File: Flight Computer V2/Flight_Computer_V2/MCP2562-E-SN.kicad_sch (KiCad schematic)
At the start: 2 parts, among them U3 MCP2562-E-SN

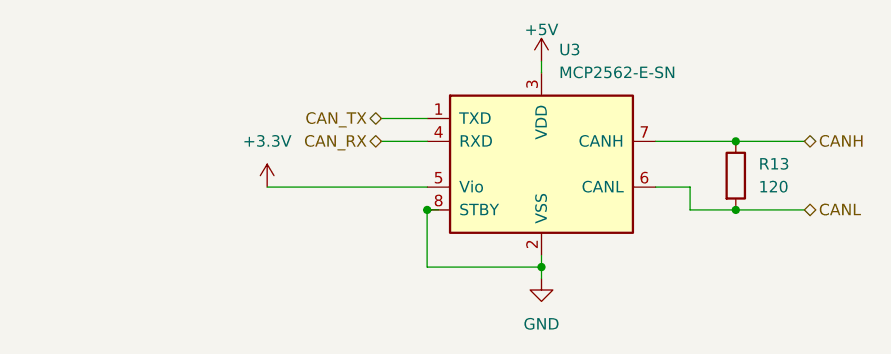
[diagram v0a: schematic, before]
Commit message: added more sensors to flight computer v2
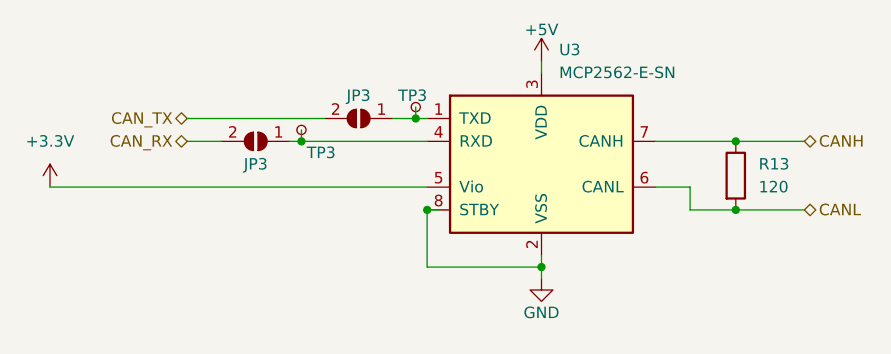
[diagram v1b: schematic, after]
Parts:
- added JP3 (x2): ~, symbol Jumper:SolderJumper_2_Open
- added TP3 (x2): TestPoint_Small, symbol Connector:TestPoint_Small
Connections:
- net CAN_RX: now also JP3.2 (B); no longer U3.4 (RXD)
- net CAN_TX: now also JP3.2 (B); no longer U3.1 (TXD)
- new net: JP3.1 (A), TP3.1, U3.1 (TXD)
- new net: JP3.1 (A), TP3.1, U3.4 (RXD)
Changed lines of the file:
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@@
   (junction (at 153.67 99.06) (diameter 0) (color 0 0 0 0)
   )
+  (junction (at 118.11 88.9) (diameter 0) (color 0 0 0 0)
+  )
+  (junction (at 105.41 91.44) (diameter 0) (color 0 0 0 0)
+  )
   (junction (at 119.38 99.06) (diameter 0) (color 0 0 0 0)
   )
+  (wire (pts (xy 115.57 88.9) (xy 118.11 88.9))
+    (stroke (width 0) (type default))
+  )
   (wire (pts (xy 132.08 82.55) (xy 132.08 83.82))
     (stroke (width 0) (type default))
@@
     (stroke (width 0) (type default))
   )
+  (wire (pts (xy 104.14 91.44) (xy 105.41 91.44))
+    (stroke (width 0) (type default))
+  )
   (wire (pts (xy 119.38 105.41) (xy 132.08 105.41))
     (stroke (width 0) (type default))
   )
+  (wire (pts (xy 105.41 91.44) (xy 119.38 91.44))
+    (stroke (width 0) (type default))
+  )
   (wire (pts (xy 144.78 96.52) (xy 148.59 96.52))
     (stroke (width 0) (type default))
@@
     (stroke (width 0) (type default))
   )
-  (wire (pts (xy 101.6 96.52) (xy 119.38 96.52))
-    (stroke (width 0) (type default))
-  )
-  (wire (pts (xy 114.3 88.9) (xy 119.38 88.9))
+  (wire (pts (xy 92.71 88.9) (xy 107.95 88.9))
+    (stroke (width 0) (type default))
+  )
+  (wire (pts (xy 105.41 90.17) (xy 105.41 91.44))
+    (stroke (width 0) (type default))
+  )
+  (wire (pts (xy 118.11 87.63) (xy 118.11 88.9))
+    (stroke (width 0) (type default))
+  )
+  (wire (pts (xy 118.11 88.9) (xy 119.38 88.9))
     (stroke (width 0) (type default))
   )
@@
     (stroke (width 0) (type default))
   )
+  (wire (pts (xy 77.47 96.52) (xy 119.38 96.52))
+    (stroke (width 0) (type default))
+  )
   (wire (pts (xy 148.59 99.06) (xy 153.67 99.06))
     (stroke (width 0) (type default))
   )
-  (wire (pts (xy 114.3 91.44) (xy 119.38 91.44))
+  (wire (pts (xy 92.71 91.44) (xy 96.52 91.44))
     (stroke (width 0) (type default))
   )
@@
     (effects (font (size 1.27 1.27)) (justify left))
   )
-  (hierarchical_label "CAN_TX" (shape bidirectional) (at 114.3 88.9 180) (fields_autoplaced)
+  (hierarchical_label "CAN_TX" (shape bidirectional) (at 92.71 88.9 180) (fields_autoplaced)
     (effects (font (size 1.27 1.27)) (justify right))
   )
@@
     (effects (font (size 1.27 1.27)) (justify left))
   )
-  (hierarchical_label "CAN_RX" (shape bidirectional) (at 114.3 91.44 180) (fields_autoplaced)
+  (hierarchical_label "CAN_RX" (shape bidirectional) (at 92.71 91.44 180) (fields_autoplaced)
     (effects (font (size 1.27 1.27)) (justify right))
   )
@@
     )
   )
+  (symbol (lib_id "Connector:TestPoint_Small") (at 105.41 90.17 180) (unit 1)
+    (in_bom yes) (on_board yes) (dnp no)
+    (property "Reference" "TP3" (at 109.22 92.71 0)
+      (effects (font (size 1.27 1.27)) (justify left))
+    )
+    (property "Value" "TestPoint_Small" (at 104.14 88.9 0)
+      (effects (font (size 1.27 1.27)) (justify left) hide)
+    )
+    (property "Footprint" "" (at 100.33 90.17 0)
+      (effects (font (size 1.27 1.27)) hide)
+    )
+    (property "Datasheet" "~" (at 100.33 90.17 0)
+      (effects (font (size 1.27 1.27)) hide)
+    )
+    (pin "1")
+    (instances
+      (project "Flight_Computer_V2"
+        (path "/39d7ebb3-b69d-4ae9-8f55-c9acfe77d345/18b8eda5-ab3e-431c-bc45-74a94283215a"
+          (reference "TP3") (unit 1)
+        )
+        (path "/39d7ebb3-b69d-4ae9-8f55-c9acfe77d345/36f68de3-e25f-423d-b7f8-c15e88151435"
+          (reference "TP5") (unit 1)
+        )
+      )
+    )
+  )
   (symbol (lib_id "power:+5V") (at 132.08 82.55 0) (unit 1)
     (in_bom yes) (on_board yes) (dnp no) (fields_autoplaced)
@@
     )
   )
-  (symbol (lib_id "power:+3.3V") (at 101.6 96.52 0) (unit 1)
-    (in_bom yes) (on_board yes) (dnp no)
-    (property "Reference" "#PWR019" (at 101.6 100.33 0)
-      (effects (font (size 1.27 1.27)) hide)
-    )
-    (property "Value" "+3.3V" (at 101.6 91.44 0)
-      (effects (font (size 1.27 1.27)))
-    )
-    (property "Footprint" "" (at 101.6 96.52 0)
-      (effects (font (size 1.27 1.27)) hide)
-    )
-    (property "Datasheet" "" (at 101.6 96.52 0)
+  (symbol (lib_id "power:+3.3V") (at 77.47 96.52 0) (unit 1)
+    (in_bom yes) (on_board yes) (dnp no)
+    (property "Reference" "#PWR019" (at 77.47 100.33 0)
+      (effects (font (size 1.27 1.27)) hide)
+    )
+    (property "Value" "+3.3V" (at 77.47 91.44 0)
+      (effects (font (size 1.27 1.27)))
+    )
+    (property "Footprint" "" (at 77.47 96.52 0)
+      (effects (font (size 1.27 1.27)) hide)
+    )
+    (property "Datasheet" "" (at 77.47 96.52 0)
       (effects (font (size 1.27 1.27)) hide)
     )
@@
         (path "/b1d299c5-d712-4abd-abfc-85bf9dc0241e/b49ccfa2-a443-40e6-a4d4-e4cbe0c6bead"
           (reference "#PWR042") (unit 1)
+        )
+      )
+    )
+  )
+  (symbol (lib_id "Jumper:SolderJumper_2_Open") (at 100.33 91.44 180) (unit 1)
+    (in_bom yes) (on_board yes) (dnp no)
+    (property "Reference" "JP3" (at 100.33 93.98 0)
+      (effects (font (size 1.27 1.27)))
+    )
+    (property "Value" "~" (at 100.33 95.25 0)
+      (effects (font (size 1.27 1.27)))
+    )
+    (property "Footprint" "" (at 100.33 91.44 0)
+      (effects (font (size 1.27 1.27)) hide)
+    )
+    (property "Datasheet" "~" (at 100.33 91.44 0)
+      (effects (font (size 1.27 1.27)) hide)
+    )
+    (pin "1")
+    (pin "2")
+    (instances
+      (project "Flight_Computer_V2"
+        (path "/39d7ebb3-b69d-4ae9-8f55-c9acfe77d345/18b8eda5-ab3e-431c-bc45-74a94283215a"
+          (reference "JP3") (unit 1)
+        )
+        (path "/39d7ebb3-b69d-4ae9-8f55-c9acfe77d345/36f68de3-e25f-423d-b7f8-c15e88151435"
+          (reference "JP5") (unit 1)
         )
       )
@@
   )
   (symbol (lib_id "power:GND") (at 132.08 106.68 0) (unit 1)
-    (in_bom yes) (on_board yes) (dnp no) (fields_autoplaced)
+    (in_bom yes) (on_board yes) (dnp no)
     (property "Reference" "#PWR020" (at 132.08 113.03 0)
       (effects (font (size 1.27 1.27)) hide)
     )
-    (property "Value" "GND" (at 132.08 111.76 0)
+    (property "Value" "GND" (at 132.08 110.49 0)
       (effects (font (size 1.27 1.27)))
     )
@@
         )
       )
+    )
+  )
+  (symbol (lib_id "Connector:TestPoint_Small") (at 118.11 87.63 180) (unit 1)
+    (in_bom yes) (on_board yes) (dnp no)
+    (property "Reference" "TP3" (at 119.38 86.36 0)
+      (effects (font (size 1.27 1.27)) (justify left))
+    )
+    (property "Value" "TestPoint_Small" (at 116.84 86.36 0)
+      (effects (font (size 1.27 1.27)) (justify left) hide)
+    )
+    (property "Footprint" "" (at 113.03 87.63 0)
+      (effects (font (size 1.27 1.27)) hide)
+    )
+    (property "Datasheet" "~" (at 113.03 87.63 0)
+      (effects (font (size 1.27 1.27)) hide)
+    )
+    (pin "1")
+    (instances
+      (project "Flight_Computer_V2"
+        (path "/39d7ebb3-b69d-4ae9-8f55-c9acfe77d345/18b8eda5-ab3e-431c-bc45-74a94283215a"
+          (reference "TP3") (unit 1)
+        )
+        (path "/39d7ebb3-b69d-4ae9-8f55-c9acfe77d345/36f68de3-e25f-423d-b7f8-c15e88151435"
+          (reference "TP4") (unit 1)
+        )
+      )
+    )
+  )
+  (symbol (lib_id "Jumper:SolderJumper_2_Open") (at 111.76 88.9 180) (unit 1)
+    (in_bom yes) (on_board yes) (dnp no)
+    (property "Reference" "JP3" (at 111.76 86.36 0)
+      (effects (font (size 1.27 1.27)))
+    )
+    (property "Value" "~" (at 111.76 92.71 0)
+      (effects (font (size 1.27 1.27)))
+    )
+    (property "Footprint" "" (at 111.76 88.9 0)
+      (effects (font (size 1.27 1.27)) hide)
+    )
+    (property "Datasheet" "~" (at 111.76 88.9 0)
+      (effects (font (size 1.27 1.27)) hide)
+    )
+    (pin "1")
+    (pin "2")
+    (instances
+      (project "Flight_Computer_V2"
+        (path "/39d7ebb3-b69d-4ae9-8f55-c9acfe77d345/18b8eda5-ab3e-431c-bc45-74a94283215a"
+          (reference "JP3") (unit 1)
+        )
+        (path "/39d7ebb3-b69d-4ae9-8f55-c9acfe77d345/36f68de3-e25f-423d-b7f8-c15e88151435"
+          (reference "JP4") (unit 1)
+        )
+      )

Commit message: finalized schematic, added datasheets, and pdf of schematic
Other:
- company: (none) -> By: Dylan Haussecker
- title: (none) -> Avionics Flight Computer
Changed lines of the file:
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@@
 (kicad_sch (version 20230121) (generator eeschema)
   (paper "A4")
+  (title_block
+    (title "Avionics Flight Computer")
+    (date "2023-09-04")
+    (rev "1.0")
+    (company "By: Dylan Haussecker")
+  )
   (junction (at 132.08 105.41) (diameter 0) (color 0 0 0 0)
   )

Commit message: updated pcb
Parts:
- JP3: footprint (none) -> Jumper:SolderJumper-2_P1.3mm_Open_Pad1.0x1.5mm
- R13: footprint (none) -> Resistor_SMD:R_0603_1608Metric
- TP3: footprint (none) -> TestPoint:TestPoint_Pad_D1.0mm
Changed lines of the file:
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@@
       (effects (font (size 1.27 1.27)) (justify left) hide)
     )
-    (property "Footprint" "" (at 100.33 90.17 0)
+    (property "Footprint" "TestPoint:TestPoint_Pad_D1.0mm" (at 100.33 90.17 0)
       (effects (font (size 1.27 1.27)) hide)
     )
@@
   (symbol (lib_id "power:+3.3V") (at 77.47 96.52 0) (unit 1)
     (in_bom yes) (on_board yes) (dnp no)
-    (property "Reference" "#PWR019" (at 77.47 100.33 0)
+    (property "Reference" "#PWR0108" (at 77.47 100.33 0)
       (effects (font (size 1.27 1.27)) hide)
     )
@@
       (project "Flight_Computer_V2"
         (path "/39d7ebb3-b69d-4ae9-8f55-c9acfe77d345/36f68de3-e25f-423d-b7f8-c15e88151435"
-          (reference "#PWR019") (unit 1)
+          (reference "#PWR0108") (unit 1)
         )
       )
@@
       (effects (font (size 1.27 1.27)))
     )
-    (property "Footprint" "" (at 100.33 91.44 0)
+    (property "Footprint" "Jumper:SolderJumper-2_P1.3mm_Open_Pad1.0x1.5mm" (at 100.33 91.44 0)
       (effects (font (size 1.27 1.27)) hide)
     )
@@
       (effects (font (size 1.27 1.27)) (justify left))
     )
-    (property "Footprint" "" (at 151.892 95.25 90)
+    (property "Footprint" "Resistor_SMD:R_0603_1608Metric" (at 151.892 95.25 90)
       (effects (font (size 1.27 1.27)) hide)
     )
@@
   (symbol (lib_id "power:GND") (at 132.08 106.68 0) (unit 1)
     (in_bom yes) (on_board yes) (dnp no)
-    (property "Reference" "#PWR020" (at 132.08 113.03 0)
+    (property "Reference" "#PWR0107" (at 132.08 113.03 0)
       (effects (font (size 1.27 1.27)) hide)
     )
@@
       (project "Flight_Computer_V2"
         (path "/39d7ebb3-b69d-4ae9-8f55-c9acfe77d345/36f68de3-e25f-423d-b7f8-c15e88151435"
-          (reference "#PWR020") (unit 1)
+          (reference "#PWR0107") (unit 1)
         )
       )
@@
       (effects (font (size 1.27 1.27)) (justify left) hide)
     )
-    (property "Footprint" "" (at 113.03 87.63 0)
+    (property "Footprint" "TestPoint:TestPoint_Pad_D1.0mm" (at 113.03 87.63 0)
       (effects (font (size 1.27 1.27)) hide)
     )
@@
       (effects (font (size 1.27 1.27)))
     )
-    (property "Footprint" "" (at 111.76 88.9 0)
-      (effects (font (size 1.27 1.27)) hide)
-    )
+    (property "Footprint" "Jumper:SolderJumper-2_P1.3mm_Open_Pad1.0x1.5mm" (at 111.76 88.9 0)
+      (effects (font (size 1.27 1.27)) hide)
+    )
